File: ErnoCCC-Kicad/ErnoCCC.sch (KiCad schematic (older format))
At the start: 85 parts, among them J1 6VAC, J2 ICSP, J3 FTDI, J4 Erno Controller, J5 SWITCH, J6 LED OUT, J7 Conn_01x07, Q1 BC847, Q2 BC847, SW1 SW_Push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

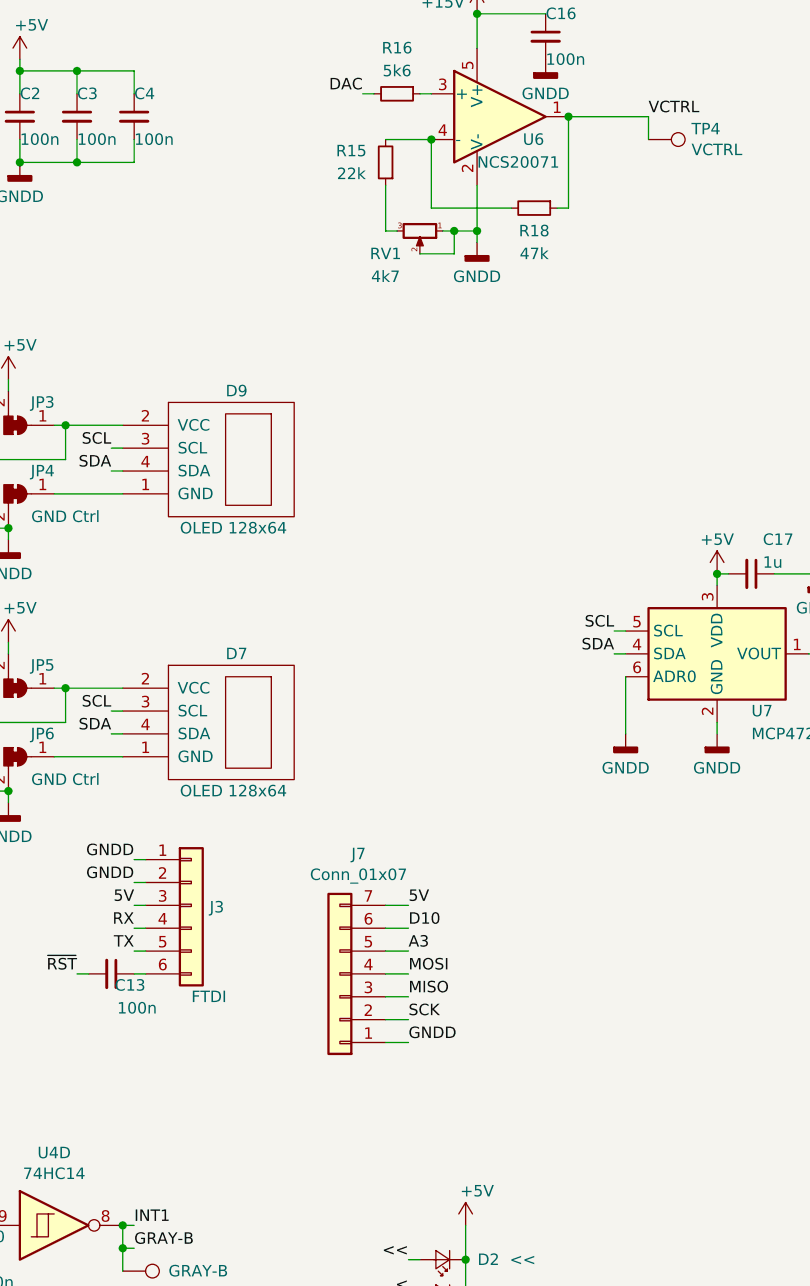
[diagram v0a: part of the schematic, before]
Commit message: Adding I2C on a pinheader
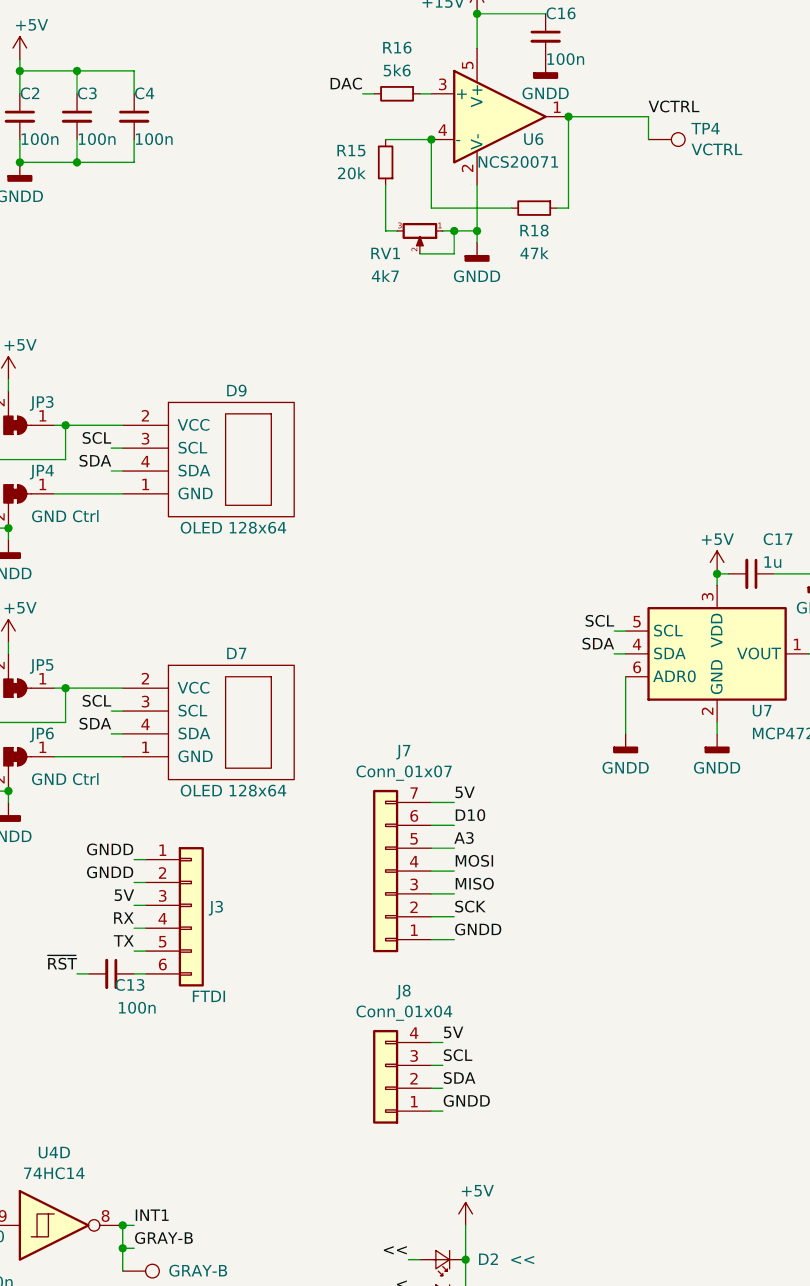
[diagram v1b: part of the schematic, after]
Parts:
- added J8: Conn_01x04, Connector_PinHeader_2.54mm:PinHeader_1x04_P2.54mm_Vertical, symbol Connector_Generic:Conn_01x04
- J7: footprint Connector_PinHeader_2.54mm:PinHeader_1x05_P2.54mm_Horizontal_shorter -> Connector_PinSocket_2.54mm:PinSocket_1x07_P2.54mm_Vertical
- R15: value 22k -> 20k
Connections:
- net +5V: now also J8.4 (Pin_4)
- net GND: now also J8.1 (Pin_1)
- net SCL: now also J8.3 (Pin_3)
- net SDA: now also J8.2 (Pin_2)
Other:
- moved on the sheet: J7
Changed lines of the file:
@@
 L Connector_Generic:Conn_01x07 J7
 U 1 1 5E107107
-P 5400 4900
-F 0 "J7" H 5318 4375 50  0000 C CNN
-F 1 "Conn_01x07" H 5318 4466 50  0000 C CNN
-F 2 "Connector_PinHeader_2.54mm:PinHeader_1x05_P2.54mm_Horizontal_shorter" H 5400 4900 50  0001 C CNN
-F 3 "~" H 5400 4900 50  0001 C CNN
-	1    5400 4900
+P 5600 4450
+F 0 "J7" H 5518 3925 50  0000 C CNN
+F 1 "Conn_01x07" H 5518 4016 50  0000 C CNN
+F 2 "Connector_PinSocket_2.54mm:PinSocket_1x07_P2.54mm_Vertical" H 5600 4450 50  0001 C CNN
+F 3 "~" H 5600 4450 50  0001 C CNN
+	1    5600 4450
 	-1   0    0    1
 $EndComp
-Text Label 5700 4700 0    50   ~ 0
+Text Label 5900 4250 0    50   ~ 0
 D10
 Text Label 4550 7200 0    50   ~ 0
@@
 	4450 6100 4500 6100
 Wire Wire Line
-	5600 4700 5700 4700
-Wire Wire Line
-	5600 5000 5700 5000
-Wire Wire Line
-	5600 5100 5700 5100
+	5800 4250 5900 4250
+Wire Wire Line
+	5800 4550 5900 4550
+Wire Wire Line
+	5800 4650 5900 4650
 $Comp
 L Jumper:SolderJumper_3_Bridged12 JP3
@@
 P 5600 1350
 F 0 "R15" H 5750 1300 50  0000 C CNN
-F 1 "22k" H 5750 1400 50  0000 C CNN
+F 1 "20k" H 5750 1400 50  0000 C CNN
 F 2 "Resistor_SMD:R_0805_2012Metric" H 5600 1350 50  0001 C CNN
 F 3 "~" H 5600 1350 50  0001 C CNN
@@
 Wire Wire Line
 	7450 3500 7500 3500
-Text Label 6600 3500 2    50   ~ 0
-SDA
-Text Label 6600 3400 2    50   ~ 0
-SCL
 $Comp
 L Device:C_Small C17
@@
 	2000 2600 2150 2600
 Wire Wire Line
-	5600 4800 5700 4800
-Wire Wire Line
-	5600 4900 5700 4900
+	5800 4350 5900 4350
+Wire Wire Line
+	5800 4450 5900 4450
 $Comp
 L Device:CP_Small C18
@@
 	10050 2800 10050 2900
 Connection ~ 10050 2900
-Wire Wire Line
-	6650 3400 6600 3400
-Wire Wire Line
-	6650 3500 6600 3500
 $Comp
 L Device:D_Schottky_Small D10
@@
 Wire Wire Line
 	6650 3600 6650 3850
-Text Label 5700 4900 0    50   ~ 0
+Text Label 5900 4450 0    50   ~ 0
 MOSI
-Text Label 5700 5000 0    50   ~ 0
+Text Label 5900 4550 0    50   ~ 0
 MISO
-Text Label 5700 5100 0    50   ~ 0
+Text Label 5900 4650 0    50   ~ 0
 SCK
 Text Label 2150 3600 0    50   ~ 0
 A3
-Text Label 5700 4800 0    50   ~ 0
+Text Label 5900 4350 0    50   ~ 0
 A3
 $Comp
@@
 Wire Wire Line
 	6750 1150 6750 1250
-Text Label 5700 4600 0    50   ~ 0
+Text Label 5900 4150 0    50   ~ 0
 5V
-Text Label 5700 5200 0    50   ~ 0
+Text Label 5900 4750 0    50   ~ 0
 GNDD
 Wire Wire Line
-	5600 4600 5700 4600
-Wire Wire Line
-	5600 5200 5700 5200
+	5800 4150 5900 4150
+Wire Wire Line
+	5800 4750 5900 4750
 $Comp
 L Connector:TestPoint TP7
@@
 	8900 2900 8900 3000
 Connection ~ 8900 3000
+Wire Wire Line
+	6650 3500 6600 3500
+Wire Wire Line
+	6650 3400 6600 3400
+Text Label 6600 3500 2    50   ~ 0
+SDA
+Text Label 6600 3400 2    50   ~ 0
+SCL
+$Comp
+L Connector_Generic:Conn_01x04 J8
+U 1 1 5E81FCAC
+P 5600 5400
+F 0 "J8" H 5518 4975 50  0000 C CNN
+F 1 "Conn_01x04" H 5518 5066 50  0000 C CNN
+F 2 "Connector_PinHeader_2.54mm:PinHeader_1x04_P2.54mm_Vertical" H 5600 5400 50  0001 C CNN
+F 3 "~" H 5600 5400 50  0001 C CNN
+	1    5600 5400
+	-1   0    0    1
+$EndComp
+Text Label 5850 5300 0    50   ~ 0
+SCL
+Text Label 5850 5400 0    50   ~ 0
+SDA
+Text Label 5850 5500 0    50   ~ 0
+GNDD
+Text Label 5850 5200 0    50   ~ 0
+5V
+Wire Wire Line
+	5800 5200 5850 5200
+Wire Wire Line
+	5800 5300 5850 5300
+Wire Wire Line
+	5800 5400 5850 5400
+Wire Wire Line
+	5800 5500 5850 5500
 $EndSCHEMATC

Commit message: RevC: Done!
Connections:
- net +5V: now also J8.2 (Pin_2); no longer J8.4 (Pin_4)
- net SDA: now also J8.4 (Pin_4); no longer J8.2 (Pin_2)
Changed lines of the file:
@@
 Text Label 5850 5300 0    50   ~ 0
 SCL
-Text Label 5850 5400 0    50   ~ 0
+Text Label 5850 5200 0    50   ~ 0
 SDA
 Text Label 5850 5500 0    50   ~ 0
 GNDD
-Text Label 5850 5200 0    50   ~ 0
+Text Label 5850 5400 0    50   ~ 0
 5V
 Wire Wire Line

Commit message: Fixing the short in the LEDs :(
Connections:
- net +5V: no longer D2.1 (K), D3.1 (K), D4.1 (K), D5.1 (K), D6.1 (K), R14.1
- new net: D2.1 (K), D3.1 (K), D4.1 (K), D5.1 (K), D6.1 (K), R14.1
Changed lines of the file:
@@
-$EndComp
-Wire Wire Line
-	5950 6000 5950 6150
-Connection ~ 5950 6150
-$Comp
-L power:+5V #PWR025
-U 1 1 6022183D
-P 5950 6000
-F 0 "#PWR025" H 5950 5850 50  0001 C CNN
-F 1 "+5V" H 6000 6150 50  0000 C CNN
-F 2 "" H 5950 6000 50  0001 C CNN
-F 3 "" H 5950 6000 50  0001 C CNN
-	1    5950 6000
-	1    0    0    -1
 $EndComp
 Wire Wire Line
